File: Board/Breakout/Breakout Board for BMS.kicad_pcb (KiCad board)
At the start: 2 copper layers, 63.9 x 51.4 mm, 16 parts, among them J1 Conn_01x04, J11 Conn_01x02, J4 Conn_01x03, J7 Conn_01x05, J9 Conn_01x02

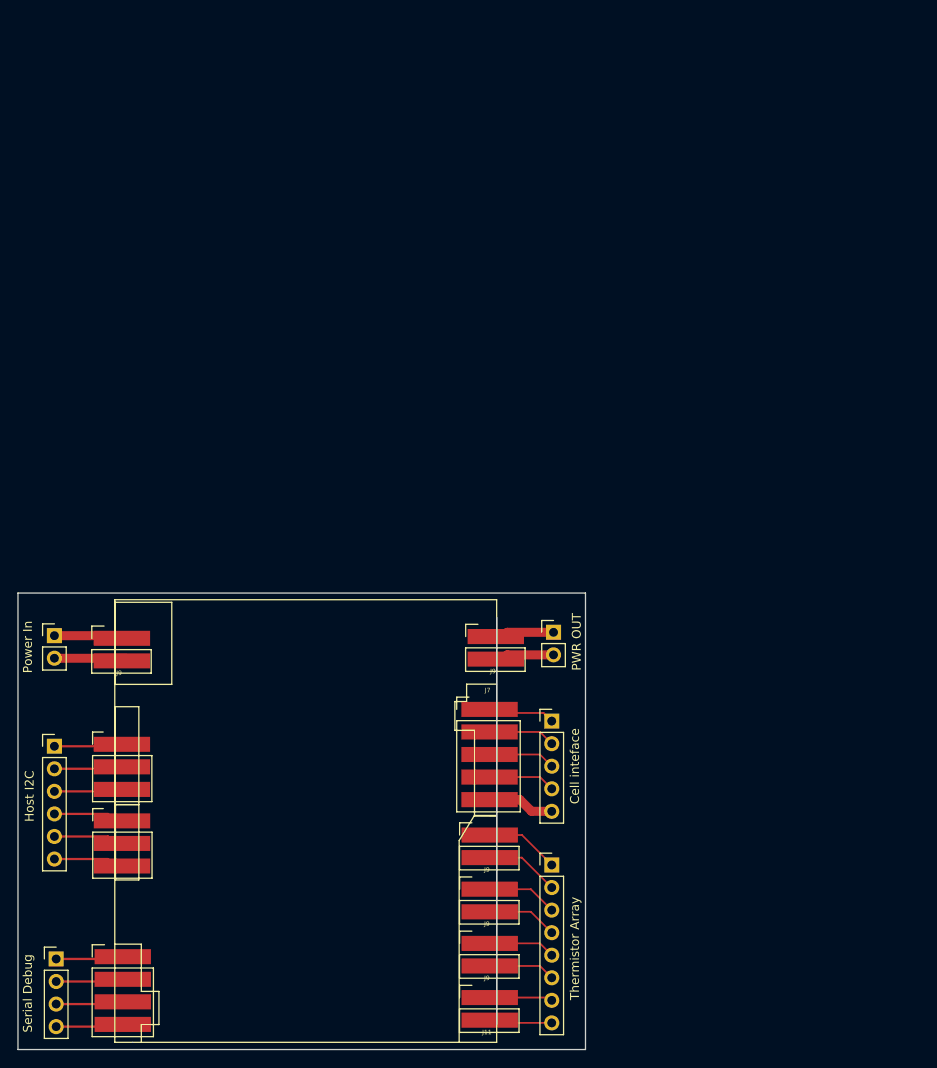
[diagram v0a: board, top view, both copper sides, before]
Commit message: Breakout Board updated
Added ground zones, fixed issues with malformed board
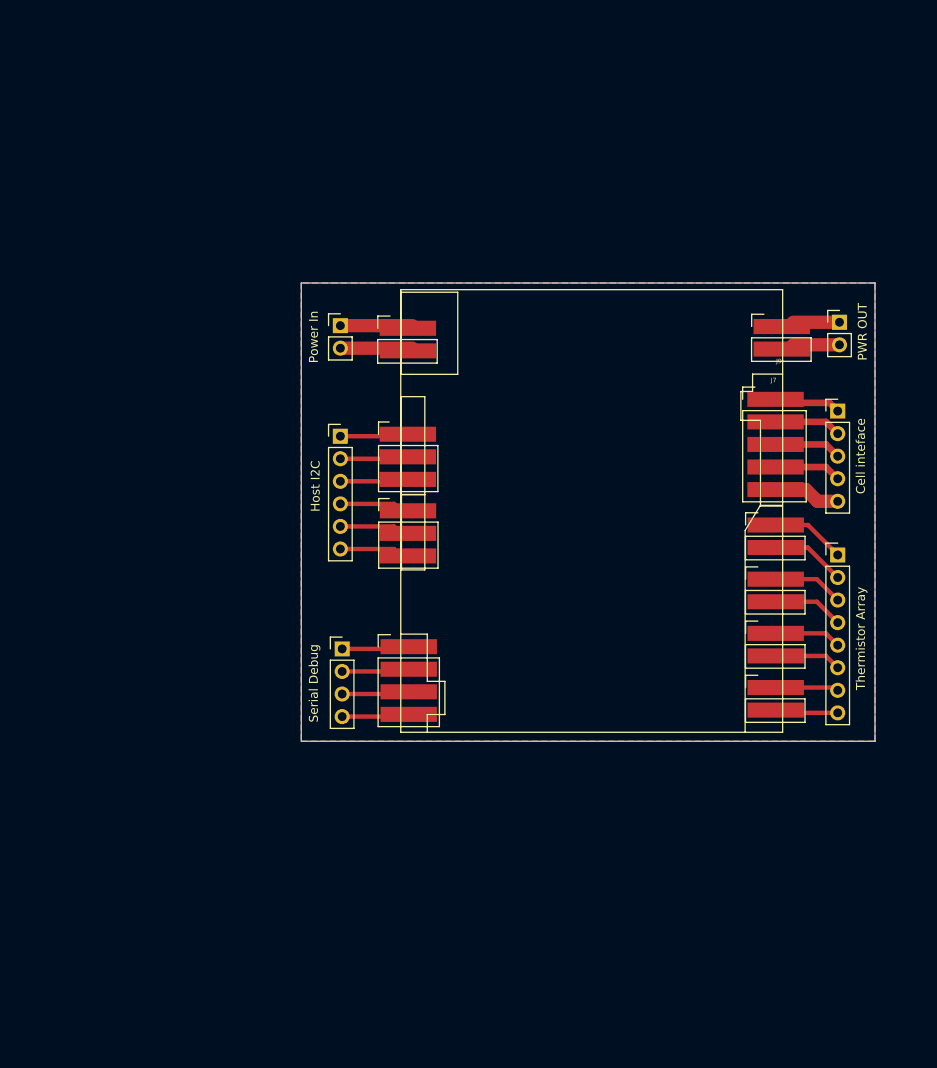
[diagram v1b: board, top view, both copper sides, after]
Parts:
- moved J9 47.5 mm to (166.3, 67.0)
- moved Thermistor Array 47.5 mm to (171.8, 92.7)
- moved Cell inteface 47.5 mm to (171.8, 76.5)
- moved Host I2C 47.5 mm to (115.8, 79.3)
- moved J11 47.5 mm to (165.6, 107.6)
- moved J4 47.5 mm to (122.6, 87.7)
- moved J9 47.5 mm to (124.2, 67.2)
- moved Power In 47.5 mm to (115.8, 66.9)
- moved J4 47.5 mm to (122.6, 79.1)
- moved J7 47.5 mm to (165.6, 75.2)
- moved J9 47.5 mm to (165.6, 89.3)
- moved J9 47.5 mm to (165.6, 95.4)
- moved PWR OUT 47.5 mm to (172.0, 66.5)
- moved J1 47.5 mm to (122.7, 103.0)
- moved Serial Debug 47.5 mm to (116.0, 103.3)
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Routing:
- added copper zone on B.Cu, net (none)
- added copper zone on F.Cu, net (none)
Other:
- board size 63.9 x 51.4 mm -> 64.6 x 51.6 mm

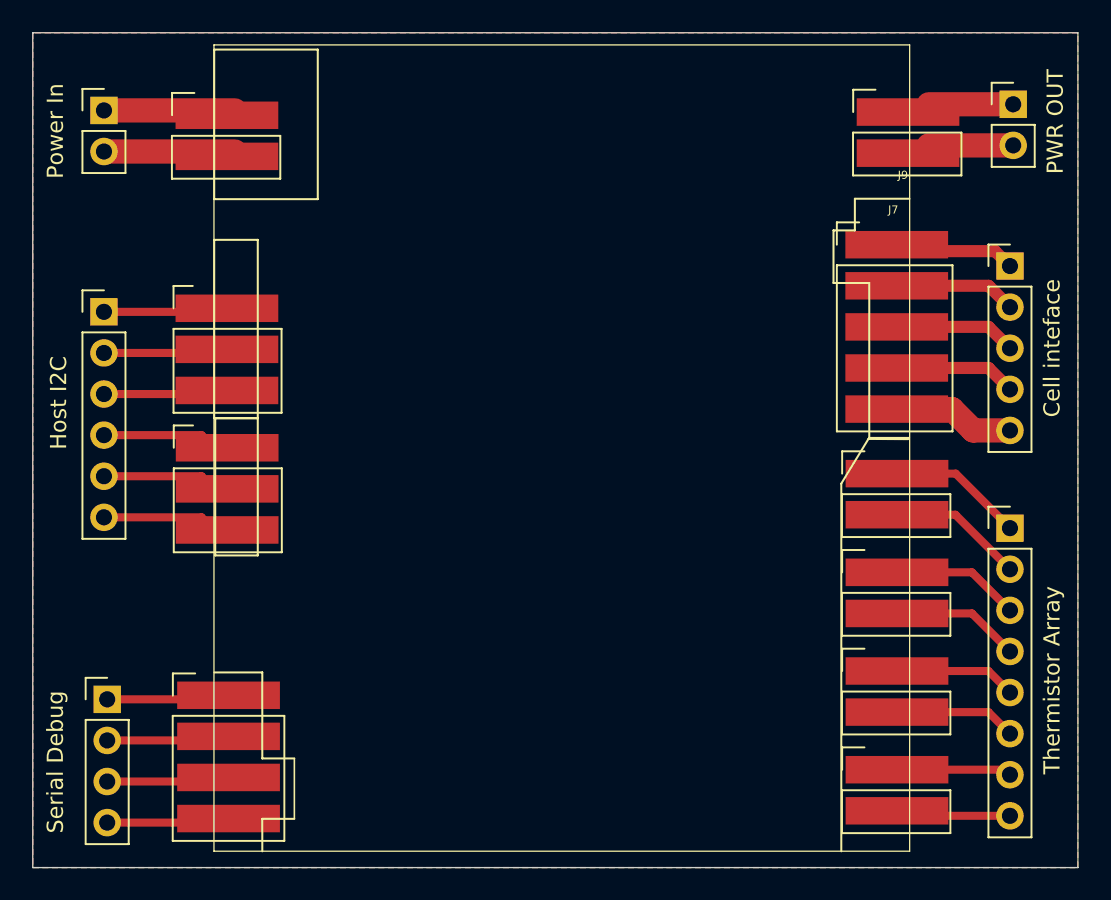
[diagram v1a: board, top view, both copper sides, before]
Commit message: Ground zone for Breakout filled
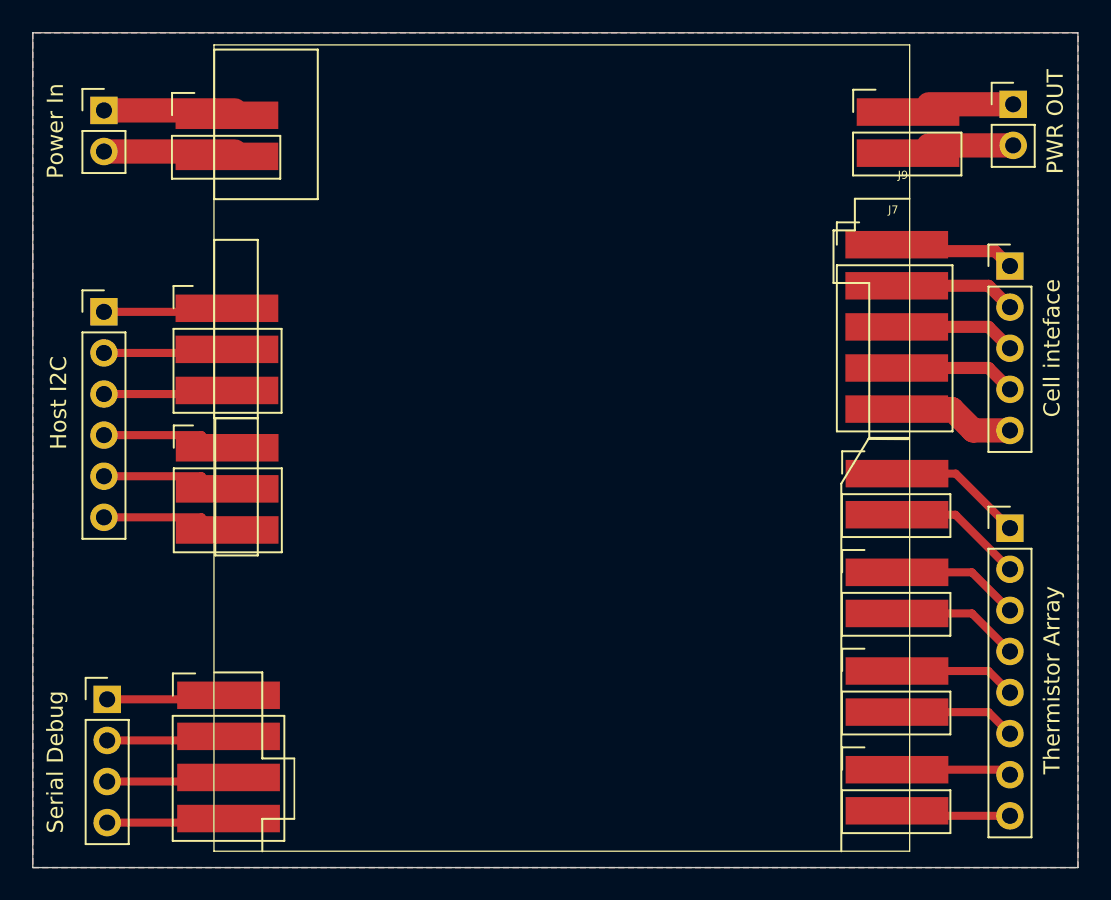
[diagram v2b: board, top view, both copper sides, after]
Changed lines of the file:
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@@
 		(min_thickness 0.25)
 		(filled_areas_thickness no)
-		(fill
+		(fill yes
 			(thermal_gap 0.5)
 			(thermal_bridge_width 0.5)
 			(smoothing fillet)
+			(radius 2.5)
 			(island_removal_mode 1)
 			(island_area_min 10)
@@
 			)
 		)
+	)
+	(zone
+		(net 0)
+		(net_name "")
+		(layer "B.Cu")
+		(name "Ground Flood")
+		(hatch edge 0.5)
+		(priority 1)
+		(connect_pads
+			(clearance 0.5)
+		)
+		(min_thickness 0.25)
+		(filled_areas_thickness no)
+		(fill
+			(thermal_gap 0.5)
+			(thermal_bridge_width 0.5)
+			(smoothing fillet)
+			(radius 2.5)
+			(island_removal_mode 1)
+			(island_area_min 10)
+		)
+		(polygon
+			(pts
+				(xy 176 62.09) (xy 111.4 62.09) (xy 111.4 113.69) (xy 176 113.69)
+			)
+		)

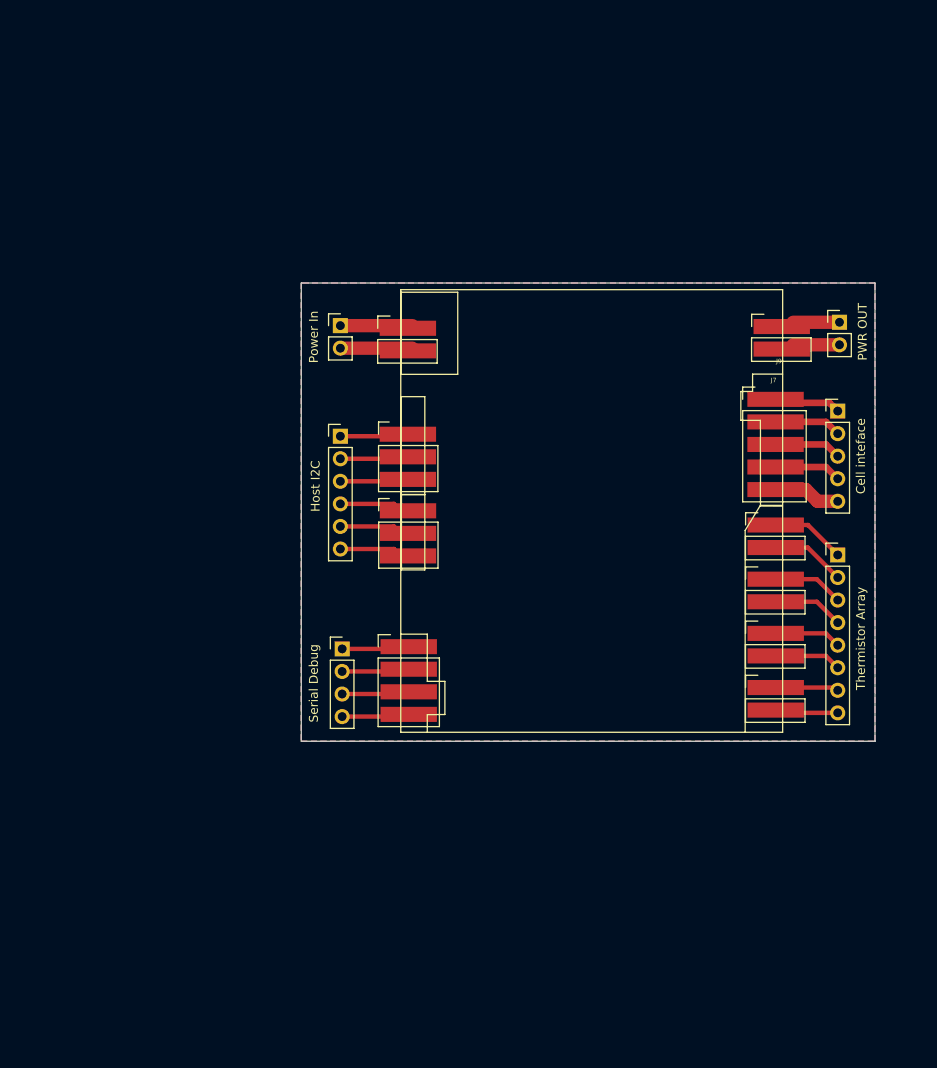
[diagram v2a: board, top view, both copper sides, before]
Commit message: Added fillet to breakoutboard
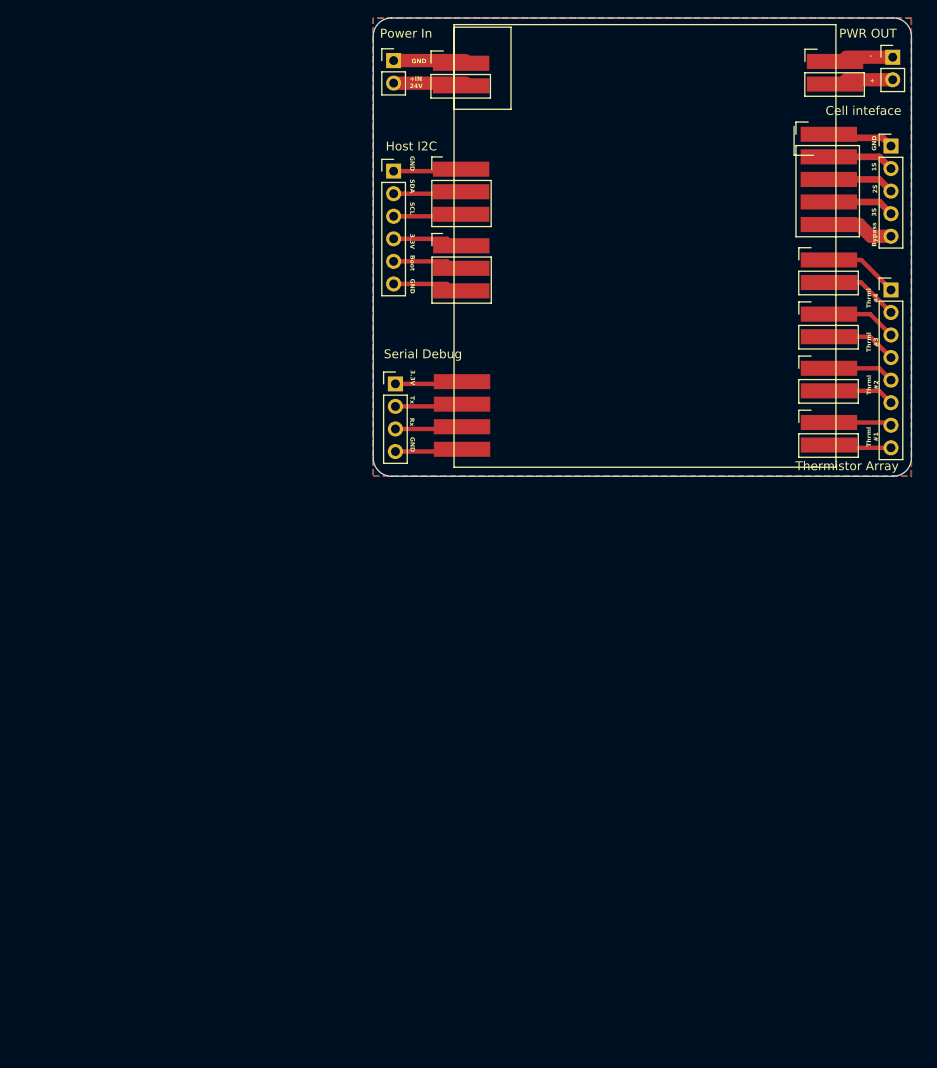
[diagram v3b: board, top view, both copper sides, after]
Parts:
- moved J4 30.4 mm to (128.6, 49.3)
- moved PWR OUT 30.4 mm to (178.0, 36.7)
- moved Cell inteface 30.4 mm to (177.8, 46.7)
- moved Host I2C 30.4 mm to (121.8, 49.5)
- moved J11 30.4 mm to (171.6, 77.8)
- moved J4 30.4 mm to (128.6, 57.9)
- moved J7 30.4 mm to (171.6, 45.3)
- moved J9 30.4 mm to (171.6, 71.7)
- moved J9 30.4 mm to (171.6, 59.5)
- moved J9 30.4 mm to (171.6, 65.6)
- moved Power In 30.4 mm to (121.8, 37.0)
- moved Serial Debug 30.4 mm to (122.0, 73.4)
- moved J1 30.4 mm to (128.7, 73.2)
- moved J9 30.4 mm to (130.2, 37.3)
- moved J9 30.4 mm to (172.3, 37.1)
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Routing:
- added copper zone on B.Cu, net gnd
- added copper zone on F.Cu, net gnd
- removed copper zone on B.Cu, net (none)
- removed copper zone on F.Cu, net (none)
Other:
- board size 64.6 x 51.6 mm -> 60.6 x 51.6 mm
- board text added: "+"
- board text added: "+IN 24V"
- board text added: "-"
- board text added: "1S"
- board text added: "2S"
- board text added: "3.3V"
- board text added: "3S"
- board text added: "Boot"
- board text added: "Bypass"
- board text added: "GND"
- board text added: "Rx"
- board text added: "SCL"
- board text added: "SDA"
- board text added: "Thrml #1"
- board text added: "Thrml #2"
- board text added: "Thrml #3"
- board text added: "Thrml #4"
- board text added: "Tx"
